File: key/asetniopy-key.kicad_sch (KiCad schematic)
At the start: 4 parts, among them J1 Conn_01x02_Female, SW1 SW_Push

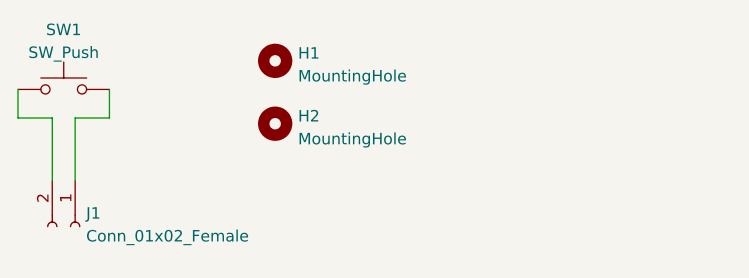
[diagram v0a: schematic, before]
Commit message: Add mouse bites for key mounting section
* Move keeb.io lib up for re-use of the submodule.
* Add second jumper to the key PCB.
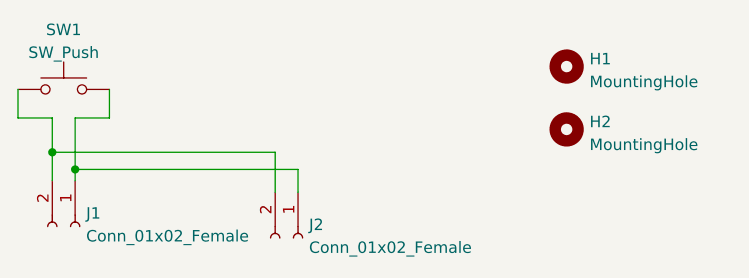
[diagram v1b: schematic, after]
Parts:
- added J2: Conn_01x02_Female, Connector_Molex:Molex_Pico-EZmate_78171-0002_1x02-1MP_P1.20mm_Vertical, symbol Connector:Conn_01x02_Female
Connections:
- net at J1.2 (Pin_2), SW1.1: now also J2.2 (Pin_2)
- net at J1.1 (Pin_1), SW1.2: now also J2.1 (Pin_1)
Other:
- moved on the sheet: H1, H2
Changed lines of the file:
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@@
 (kicad_sch (version 20211123) (generator eeschema)
   (paper "A4")
+  (junction (at 40.64 46.99) (diameter 0) (color 0 0 0 0)
+  )
+  (junction (at 43.18 48.895) (diameter 0) (color 0 0 0 0)
+  )
+  (wire (pts (xy 43.18 48.895) (xy 43.18 50.165))
+    (stroke (width 0) (type default) (color 0 0 0 0))
+  )
   (wire (pts (xy 46.99 43.18) (xy 43.18 43.18))
     (stroke (width 0) (type default) (color 0 0 0 0))
   )
-  (wire (pts (xy 43.18 43.18) (xy 43.18 50.165))
+  (wire (pts (xy 43.18 43.18) (xy 43.18 48.895))
     (stroke (width 0) (type default) (color 0 0 0 0))
   )
-  (wire (pts (xy 40.64 50.165) (xy 40.64 43.18))
+  (wire (pts (xy 40.64 50.165) (xy 40.64 46.99))
+    (stroke (width 0) (type default) (color 0 0 0 0))
+  )
+  (wire (pts (xy 67.945 48.895) (xy 67.945 51.435))
     (stroke (width 0) (type default) (color 0 0 0 0))
   )
@@
     (stroke (width 0) (type default) (color 0 0 0 0))
   )
+  (wire (pts (xy 43.18 48.895) (xy 67.945 48.895))
+    (stroke (width 0) (type default) (color 0 0 0 0))
+  )
   (wire (pts (xy 46.99 40.005) (xy 46.99 43.18))
+    (stroke (width 0) (type default) (color 0 0 0 0))
+  )
+  (wire (pts (xy 40.64 46.99) (xy 40.64 43.18))
+    (stroke (width 0) (type default) (color 0 0 0 0))
+  )
+  (wire (pts (xy 40.64 46.99) (xy 65.405 46.99))
+    (stroke (width 0) (type default) (color 0 0 0 0))
+  )
+  (wire (pts (xy 65.405 46.99) (xy 65.405 51.435))
     (stroke (width 0) (type default) (color 0 0 0 0))
   )
@@
     (stroke (width 0) (type default) (color 0 0 0 0))
   )
-  (symbol (lib_id "Mechanical:MountingHole") (at 65.405 36.83 0) (unit 1)
+  (symbol (lib_id "Mechanical:MountingHole") (at 97.79 37.465 0) (unit 1)
     (in_bom yes) (on_board yes) (fields_autoplaced)
-    (property "Reference" "H1" (id 0) (at 67.945 35.9953 0)
+    (property "Reference" "H1" (id 0) (at 100.33 36.6303 0)
       (effects (font (size 1.27 1.27)) (justify left))
     )
-    (property "Value" "MountingHole" (id 1) (at 67.945 38.5322 0)
+    (property "Value" "MountingHole" (id 1) (at 100.33 39.1672 0)
       (effects (font (size 1.27 1.27)) (justify left))
     )
-    (property "Footprint" "MountingHole:MountingHole_2.2mm_M2_Pad_TopBottom" (id 2) (at 65.405 36.83 0)
+    (property "Footprint" "MountingHole:MountingHole_2.2mm_M2_Pad_TopBottom" (id 2) (at 97.79 37.465 0)
       (effects (font (size 1.27 1.27)) hide)
     )
-    (property "Datasheet" "~" (id 3) (at 65.405 36.83 0)
+    (property "Datasheet" "~" (id 3) (at 97.79 37.465 0)
       (effects (font (size 1.27 1.27)) hide)
     )
   )
-  (symbol (lib_id "Mechanical:MountingHole") (at 65.405 43.815 0) (unit 1)
+  (symbol (lib_id "Mechanical:MountingHole") (at 97.79 44.45 0) (unit 1)
     (in_bom yes) (on_board yes) (fields_autoplaced)
-    (property "Reference" "H2" (id 0) (at 67.945 42.9803 0)
+    (property "Reference" "H2" (id 0) (at 100.33 43.6153 0)
       (effects (font (size 1.27 1.27)) (justify left))
     )
-    (property "Value" "MountingHole" (id 1) (at 67.945 45.5172 0)
+    (property "Value" "MountingHole" (id 1) (at 100.33 46.1522 0)
       (effects (font (size 1.27 1.27)) (justify left))
     )
-    (property "Footprint" "MountingHole:MountingHole_2.2mm_M2_Pad_TopBottom" (id 2) (at 65.405 43.815 0)
+    (property "Footprint" "MountingHole:MountingHole_2.2mm_M2_Pad_TopBottom" (id 2) (at 97.79 44.45 0)
       (effects (font (size 1.27 1.27)) hide)
     )
-    (property "Datasheet" "~" (id 3) (at 65.405 43.815 0)
+    (property "Datasheet" "~" (id 3) (at 97.79 44.45 0)
       (effects (font (size 1.27 1.27)) hide)
     )
@@
     (pin "2")
   )
+  (symbol (lib_id "Connector:Conn_01x02_Female") (at 67.945 56.515 270) (unit 1)
+    (in_bom yes) (on_board yes) (fields_autoplaced)
+    (property "Reference" "J2" (id 0) (at 69.1642 55.0453 90)
+      (effects (font (size 1.27 1.27)) (justify left))
+    )
+    (property "Value" "Conn_01x02_Female" (id 1) (at 69.1642 57.5822 90)
+      (effects (font (size 1.27 1.27)) (justify left))
+    )
+    (property "Footprint" "Connector_Molex:Molex_Pico-EZmate_78171-0002_1x02-1MP_P1.20mm_Vertical" (id 2) (at 67.945 56.515 0)
+      (effects (font (size 1.27 1.27)) hide)
+    )
+    (property "Datasheet" "~" (id 3) (at 67.945 56.515 0)
+      (effects (font (size 1.27 1.27)) hide)
+    )
+    (pin "1")
+    (pin "2")
+  )
   (sheet_instances
     (path "/" (page "1"))
@@
       (reference "J1") (unit 1) (value "Conn_01x02_Female") (footprint "Connector_Molex:Molex_Pico-EZmate_78171-0002_1x02-1MP_P1.20mm_Vertical")
     )
+    (path "/ff37b986-3284-431b-ad92-88224d1a5b96"
+      (reference "J2") (unit 1) (value "Conn_01x02_Female") (footprint "Connector_Molex:Molex_Pico-EZmate_78171-0002_1x02-1MP_P1.20mm_Vertical")
+    )
     (path "/845252a2-11c5-481f-8b1b-666245be2afa"
